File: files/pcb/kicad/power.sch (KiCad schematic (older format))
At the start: 27 parts

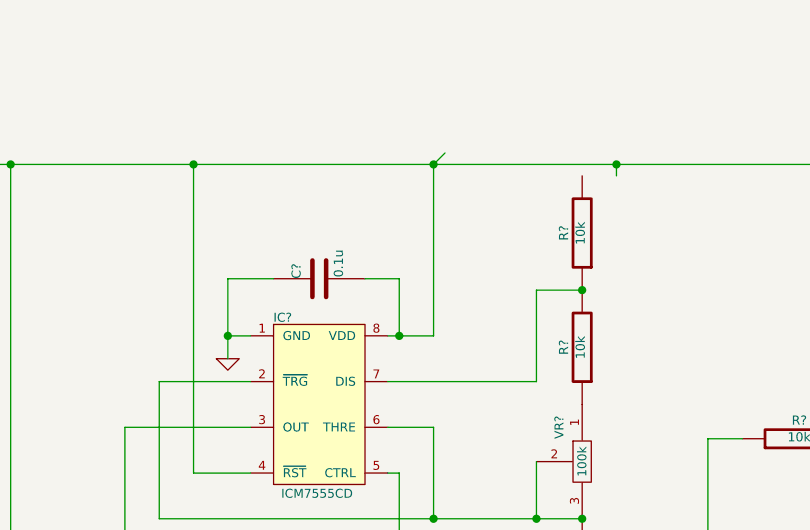
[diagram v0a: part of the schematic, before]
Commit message: 回路図更新
温度湿度センサ
大気圧センサ
輝度センサ
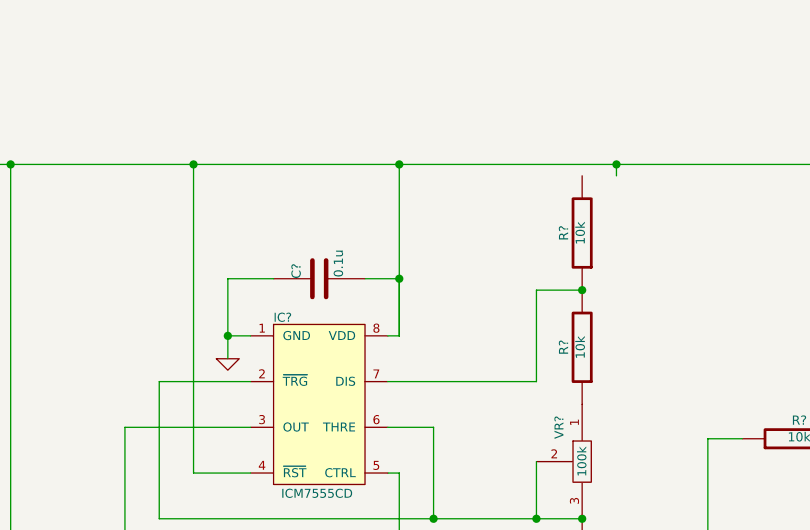
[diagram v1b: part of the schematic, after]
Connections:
- wire segments 96 -> 95
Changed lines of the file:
@@
 $EndComp
 Wire Wire Line
-	5000 3200 5000 2450
-Wire Wire Line
-	5000 2450 5050 2400
+	4850 3200 4850 2450
 Wire Wire Line
 	2650 2450 2800 2450
@@
 	3150 2450 3950 2450
 Wire Wire Line
-	3950 2450 5000 2450
-Wire Wire Line
-	5000 2450 5800 2450
+	3950 2450 4850 2450
+Wire Wire Line
+	4850 2450 5800 2450
 Wire Wire Line
 	5800 2450 7500 2450
@@
 	4800 3200 4850 3200
 Wire Wire Line
-	4850 3200 5000 3200
+	4850 3200 4850 3200
 Wire Wire Line
 	4850 3800 4800 3800
@@
 Wire Wire Line
 	5450 3400 4800 3400
-Connection ~ 4850 3200
 $Comp
 L 2SC T?
@@
 	0    -1   -1   0
 $EndComp
-Connection ~ 5000 2450
+Connection ~ 4850 2450
 Wire Wire Line
 	6350 3650 6200 3650
@@
 Connection ~ 3950 2450
 Connection ~ 5650 4400
+Connection ~ 4850 2950
 $EndSCHEMATC

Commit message: 回路図更新、DS1307対応
バスの接続が未
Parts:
- gave numbers to parts that had none: 27
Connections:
- wire segments 95 -> 97

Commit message: 回路図ERC途中
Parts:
- removed V1: 170V, symbol 170V
- added U15: DC_JACK, symbol DC_JACK
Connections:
- net labels added: 170V
- net labels removed: +9V
- wire segments 97 -> 71
- no-connect marks 0 -> 1
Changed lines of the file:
@@
 $Descr A4 11693 8268
 encoding utf-8
-Sheet 4 13
+Sheet 5 13
 Title ""
-Date "24 aug 2014"
+Date "25 aug 2014"
 Rev ""
 Comp ""
@@
 Comment4 ""
 $EndDescr
-$Comp
-L GND #PWR29
-U 1 1 53F89A11
-P 4100 3300
-F 0 "#PWR29" H 4100 3300 30  0001 C CNN
-F 1 "GND" H 4100 3230 30  0001 C CNN
-F 2 "" H 4100 3300 60  0000 C CNN
-F 3 "" H 4100 3300 60  0000 C CNN
-	1    4100 3300
-	1    0    0    -1
-$EndComp
 $Comp
 L C C8
@@
 $EndComp
 Wire Wire Line
-	4850 3200 4850 2950
-Wire Wire Line
-	4850 2950 4850 2450
-Wire Wire Line
-	2650 2450 2800 2450
-Wire Wire Line
-	2800 2450 3150 2450
-Wire Wire Line
-	3150 2450 3950 2450
-Wire Wire Line
-	3950 2450 4850 2450
-Wire Wire Line
-	4850 2450 5650 2450
-Wire Wire Line
-	5650 2450 5650 2450
-Wire Wire Line
-	5650 2450 7500 2450
-Wire Wire Line
-	7500 2450 7600 2450
+	4850 2450 4850 3200
+Wire Wire Line
+	2650 2450 7600 2450
 Wire Wire Line
 	4850 2950 4700 2950
@@
 	4300 2950 4100 2950
 Wire Wire Line
-	4100 2950 4100 3200
-Wire Wire Line
-	4100 3200 4100 3300
-Wire Wire Line
-	5650 3000 5650 3000
-Wire Wire Line
-	5650 3000 5650 3000
+	4100 2950 4100 3300
+Wire Wire Line
+	5450 3000 5650 3000
 Wire Wire Line
 	5450 4000 5450 3750
 Wire Wire Line
-	3800 4000 5000 4000
-Wire Wire Line
-	5000 4000 5450 4000
-Wire Wire Line
-	5450 4000 5650 4000
-Wire Wire Line
-	5650 4000 5650 4000
-Wire Wire Line
-	5650 4000 5650 4000
+	3800 4000 5650 4000
 Wire Wire Line
 	5650 2450 5650 2500
@@
 	5650 3500 5650 3500
 Wire Wire Line
-	4800 3200 4850 3200
-Wire Wire Line
-	4850 3200 4850 3200
+	4850 3200 4800 3200
 Wire Wire Line
 	4850 3800 4800 3800
@@
 	3650 3600 3650 4550
 Wire Wire Line
-	6900 3350 6900 3650
-Wire Wire Line
-	6900 3650 6900 3950
+	6900 3350 6900 3950
 Connection ~ 5650 4000
-Wire Wire Line
-	4850 3200 4850 2950
 Connection ~ 5650 3000
 $Comp
@@
 $EndComp
 Wire Wire Line
-	7500 3550 7500 3650
-Wire Wire Line
-	7500 3650 7500 3750
+	7500 3550 7500 3750
 Connection ~ 7500 3650
 Wire Wire Line
@@
 	7500 4200 7500 4150
 Wire Wire Line
-	7450 3650 7500 3650
-Wire Wire Line
-	7500 3650 8000 3650
+	7450 3650 8000 3650
 $Comp
 L INDUCTOR L1
@@
 Connection ~ 7500 2450
 Wire Wire Line
-	8200 2450 8300 2450
-Wire Wire Line
-	8300 2450 8400 2450
+	8200 2450 8400 2450
 Wire Wire Line
 	8300 2450 8300 3450
@@
 Connection ~ 8300 2450
 Wire Wire Line
-	8800 2450 8900 2450
-Wire Wire Line
-	8900 2450 9400 2450
-Wire Wire Line
-	9400 2450 10050 2450
+	8800 2450 10050 2450
 Wire Wire Line
 	9400 2450 9400 3450
@@
 	1    0    0    -1
 $EndComp
-Wire Wire Line
-	9400 4900 9400 3850
 $Comp
 L R R13
@@
 	8900 2450 8900 2600
 Wire Wire Line
-	8900 3650 8900 3750
-Wire Wire Line
-	8900 3750 8900 3800
+	8900 3650 8900 3800
 Wire Wire Line
 	8900 4300 8900 4350
@@
 	4850 4800 4850 3800
 Connection ~ 8900 3750
-Wire Wire Line
-	5650 3000 5450 3000
 Wire Wire Line
 	5450 3000 5450 3400
@@
 $EndComp
 $Comp
-L +9V #PWR25
-U 1 1 53F89A0B
-P 2050 2400
-F 0 "#PWR25" H 2050 2370 20  0001 C CNN
-F 1 "+9V" H 2050 2510 30  0000 C CNN
-F 2 "" H 2050 2400 60  0000 C CNN
-F 3 "" H 2050 2400 60  0000 C CNN
-	1    2050 2400
-	1    0    0    -1
-$EndComp
-$Comp
-L GND #PWR32
+L GND #PWR026
 U 1 1 53F89B53
 P 4850 5350
-F 0 "#PWR32" H 4850 5350 30  0001 C CNN
+F 0 "#PWR026" H 4850 5350 30  0001 C CNN
 F 1 "GND" H 4850 5280 30  0001 C CNN
 F 2 "" H 4850 5350 60  0000 C CNN
@@
 	4850 5200 4850 5350
 $Comp
-L GND #PWR37
+L GND #PWR027
 U 1 1 53F89C1D
 P 8900 4900
-F 0 "#PWR37" H 8900 4900 30  0001 C CNN
+F 0 "#PWR027" H 8900 4900 30  0001 C CNN
 F 1 "GND" H 8900 4830 30  0001 C CNN
 F 2 "" H 8900 4900 60  0000 C CNN
@@
 $EndComp
 $Comp
-L GND #PWR38
-U 1 1 53F89C2C
-P 9400 4900
-F 0 "#PWR38" H 9400 4900 30  0001 C CNN
-F 1 "GND" H 9400 4830 30  0001 C CNN
-F 2 "" H 9400 4900 60  0000 C CNN
-F 3 "" H 9400 4900 60  0000 C CNN
-	1    9400 4900
-	1    0    0    -1
-$EndComp
-$Comp
-L GND #PWR36
+L GND #PWR028
 U 1 1 53F89C3B
 P 8300 4200
-F 0 "#PWR36" H 8300 4200 30  0001 C CNN
+F 0 "#PWR028" H 8300 4200 30  0001 C CNN
 F 1 "GND" H 8300 4130 30  0001 C CNN
 F 2 "" H 8300 4200 60  0000 C CNN
@@
 $EndComp
 $Comp
-L GND #PWR35
+L GND #PWR029
 U 1 1 53F89C4A
 P 7500 4200
-F 0 "#PWR35" H 7500 4200 30  0001 C CNN
+F 0 "#PWR029" H 7500 4200 30  0001 C CNN
 F 1 "GND" H 7500 4130 30  0001 C CNN
 F 2 "" H 7500 4200 60  0000 C CNN
@@
 	1    0    0    -1
 $EndComp
-$Comp
-L GND #PWR34
-U 1 1 53F89C59
-P 5650 4400
-F 0 "#PWR34" H 5650 4400 30  0001 C CNN
-F 1 "GND" H 5650 4330 30  0001 C CNN
-F 2 "" H 5650 4400 60  0000 C CNN
-F 3 "" H 5650 4400 60  0000 C CNN
-	1    5650 4400
-	1    0    0    -1
-$EndComp
 Wire Wire Line
 	3950 3800 4200 3800
@@
 Connection ~ 9400 2450
 Wire Wire Line
-	6850 3650 6900 3650
-Wire Wire Line
-	6900 3650 6950 3650
+	6850 3650 6950 3650
 Connection ~ 6900 3650
 Wire Wire Line
@@
 	6200 3650 6200 4550
 $Comp
-L 170V V1
-U 1 1 53F8BBF6
-P 10050 2400
-F 0 "V1" H 10050 2400 60  0001 C CNN
-F 1 "170V" H 10060 2500 60  0000 C CNN
-F 2 "" H 10050 2400 60  0000 C CNN
-F 3 "" H 10050 2400 60  0000 C CNN
-	1    10050 2400
-	1    0    0    -1
-$EndComp
-$Comp
 L 3-TERMINAL_REGULATOR IC2
 U 1 1 53F8BD05
@@
 $EndComp
 $Comp
-L GND #PWR28
+L GND #PWR030
 U 1 1 53F8BD14
 P 3900 6450
-F 0 "#PWR28" H 3900 6450 30  0001 C CNN
+F 0 "#PWR030" H 3900 6450 30  0001 C CNN
 F 1 "GND" H 3900 6380 30  0001 C CNN
 F 2 "" H 3900 6450 60  0000 C CNN
@@
 $EndComp
 Wire Wire Line
-	4300 5950 4350 5950
-Wire Wire Line
-	4350 5950 4650 5950
-Wire Wire Line
-	4650 5950 4850 5950
+	4300 5950 4850 5950
 Wire Wire Line
 	4350 5950 4350 6000
@@
 Connection ~ 4350 5950
 Wire Wire Line
-	3150 5950 3450 5950
-Wire Wire Line
-	3450 5950 3500 5950
+	3150 5950 3500 5950
 Wire Wire Line
 	3450 5950 3450 6000
 Connection ~ 3450 5950
 $Comp
-L GND #PWR31
+L GND #PWR031
 U 1 1 53F8BED7
 P 4650 6450
-F 0 "#PWR31" H 4650 6450 30  0001 C CNN
+F 0 "#PWR031" H 4650 6450 30  0001 C CNN
 F 1 "GND" H 4650 6380 30  0001 C CNN
 F 2 "" H 4650 6450 60  0000 C CNN
@@
 $EndComp
 $Comp
-L GND #PWR30
+L GND #PWR032
 U 1 1 53F8BEE6
 P 4350 6450
-F 0 "#PWR30" H 4350 6450 30  0001 C CNN
+F 0 "#PWR032" H 4350 6450 30  0001 C CNN
 F 1 "GND" H 4350 6380 30  0001 C CNN
 F 2 "" H 4350 6450 60  0000 C CNN
@@
 $EndComp
 $Comp
-L GND #PWR27
+L GND #PWR033
 U 1 1 53F8BEF5
 P 3450 6450
-F 0 "#PWR27" H 3450 6450 30  0001 C CNN
+F 0 "#PWR033" H 3450 6450 30  0001 C CNN
 F 1 "GND" H 3450 6380 30  0001 C CNN
 F 2 "" H 3450 6450 60  0000 C CNN
@@
 $EndComp
 $Comp
-L GND #PWR26
+L GND #PWR034
 U 1 1 53F8BF04
 P 2800 3250
-F 0 "#PWR26" H 2800 3250 30  0001 C CNN
+F 0 "#PWR034" H 2800 3250 30  0001 C CNN
 F 1 "GND" H 2800 3180 30  0001 C CNN
 F 2 "" H 2800 3250 60  0000 C CNN
@@
 Connection ~ 4650 5950
 $Comp
-L +5V #PWR33
+L +5V #PWR035
 U 1 1 53F8C12B
 P 4850 5850
-F 0 "#PWR33" H 4850 5940 20  0001 C CNN
+F 0 "#PWR035" H 4850 5940 20  0001 C CNN
 F 1 "+5V" H 4850 5940 30  0000 C CNN
 F 2 "" H 4850 5850 60  0000 C CNN
@@
 $EndComp
 Wire Wire Line
-	2150 2450 2050 2450
-Wire Wire Line
-	2050 2450 2050 2400
-Wire Wire Line
 	3150 5950 3150 2450
 Connection ~ 3150 2450
@@
 	3950 3800 3950 2450
 Connection ~ 3950 2450
-Connection ~ 5650 4400
 Connection ~ 4850 2950
+$Comp
+L DC_JACK U15
+U 1 1 53FB6A7A
+P 1500 2550
+F 0 "U15" H 1350 2725 60  0000 C CNN
+F 1 "DC_JACK" H 1500 2375 60  0000 C CNN
+F 2 "" H 1350 2725 60  0000 C CNN
+F 3 "" H 1350 2725 60  0000 C CNN
+	1    1500 2550
+	1    0    0    -1
+$EndComp
+Wire Wire Line
+	1850 2650 1850 3150
+Wire Wire Line
+	1850 3150 2800 3150
+Connection ~ 2800 3150
+NoConn ~ 1850 2550
+$Comp
+L GND #PWR036
+U 1 1 53FBE781
+P 9400 4200
+F 0 "#PWR036" H 9400 4200 30  0001 C CNN
+F 1 "GND" H 9400 4130 30  0001 C CNN
+F 2 "" H 9400 4200 60  0000 C CNN
+F 3 "" H 9400 4200 60  0000 C CNN
+	1    9400 4200
+	1    0    0    -1
+$EndComp
+Wire Wire Line
+	9400 3850 9400 4200
+Text GLabel 10050 2450 2    60   Input ~ 0
+170V
+$Comp
+L GND #PWR037
+U 1 1 53FBF18E
+P 4100 3300
+F 0 "#PWR037" H 4100 3300 30  0001 C CNN
+F 1 "GND" H 4100 3230 30  0001 C CNN
+F 2 "" H 4100 3300 60  0000 C CNN
+F 3 "" H 4100 3300 60  0000 C CNN
+	1    4100 3300
+	1    0    0    -1
+$EndComp
+$Comp
+L GND #PWR038
+U 1 1 53FBF1A0
+P 5650 4450
+F 0 "#PWR038" H 5650 4450 30  0001 C CNN
+F 1 "GND" H 5650 4380 30  0001 C CNN
+F 2 "" H 5650 4450 60  0000 C CNN
+F 3 "" H 5650 4450 60  0000 C CNN
+	1    5650 4450
+	1    0    0    -1
+$EndComp
+Wire Wire Line
+	5650 4400 5650 4450
+Wire Wire Line
+	1850 2450 2150 2450
 $EndSCHEMATC

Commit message: 回路図ERC完了
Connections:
- net labels added: +9V
- wire segments 71 -> 76
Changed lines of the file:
@@
 Sheet 5 13
 Title ""
-Date "25 aug 2014"
+Date "26 aug 2014"
 Rev ""
 Comp ""
@@
 $EndComp
 $Comp
-L GND #PWR026
+L GND #PWR028
 U 1 1 53F89B53
 P 4850 5350
-F 0 "#PWR026" H 4850 5350 30  0001 C CNN
+F 0 "#PWR028" H 4850 5350 30  0001 C CNN
 F 1 "GND" H 4850 5280 30  0001 C CNN
 F 2 "" H 4850 5350 60  0000 C CNN
@@
 	4850 5200 4850 5350
 $Comp
-L GND #PWR027
+L GND #PWR029
 U 1 1 53F89C1D
 P 8900 4900
-F 0 "#PWR027" H 8900 4900 30  0001 C CNN
+F 0 "#PWR029" H 8900 4900 30  0001 C CNN
 F 1 "GND" H 8900 4830 30  0001 C CNN
 F 2 "" H 8900 4900 60  0000 C CNN
@@
 $EndComp
 $Comp
-L GND #PWR028
+L GND #PWR030
 U 1 1 53F89C3B
 P 8300 4200
-F 0 "#PWR028" H 8300 4200 30  0001 C CNN
+F 0 "#PWR030" H 8300 4200 30  0001 C CNN
 F 1 "GND" H 8300 4130 30  0001 C CNN
 F 2 "" H 8300 4200 60  0000 C CNN
@@
 $EndComp
 $Comp
-L GND #PWR029
+L GND #PWR031
 U 1 1 53F89C4A
 P 7500 4200
-F 0 "#PWR029" H 7500 4200 30  0001 C CNN
+F 0 "#PWR031" H 7500 4200 30  0001 C CNN
 F 1 "GND" H 7500 4130 30  0001 C CNN
 F 2 "" H 7500 4200 60  0000 C CNN
@@
 $EndComp
 $Comp
-L GND #PWR030
+L GND #PWR032
 U 1 1 53F8BD14
 P 3900 6450
-F 0 "#PWR030" H 3900 6450 30  0001 C CNN
+F 0 "#PWR032" H 3900 6450 30  0001 C CNN
 F 1 "GND" H 3900 6380 30  0001 C CNN
 F 2 "" H 3900 6450 60  0000 C CNN
@@
 Connection ~ 3450 5950
 $Comp
-L GND #PWR031
+L GND #PWR033
 U 1 1 53F8BED7
 P 4650 6450
-F 0 "#PWR031" H 4650 6450 30  0001 C CNN
+F 0 "#PWR033" H 4650 6450 30  0001 C CNN
 F 1 "GND" H 4650 6380 30  0001 C CNN
 F 2 "" H 4650 6450 60  0000 C CNN
@@
 $EndComp
 $Comp
-L GND #PWR032
+L GND #PWR034
 U 1 1 53F8BEE6
 P 4350 6450
-F 0 "#PWR032" H 4350 6450 30  0001 C CNN
+F 0 "#PWR034" H 4350 6450 30  0001 C CNN
 F 1 "GND" H 4350 6380 30  0001 C CNN
 F 2 "" H 4350 6450 60  0000 C CNN
@@
 $EndComp
 $Comp
-L GND #PWR033
+L GND #PWR035
 U 1 1 53F8BEF5
 P 3450 6450
-F 0 "#PWR033" H 3450 6450 30  0001 C CNN
+F 0 "#PWR035" H 3450 6450 30  0001 C CNN
 F 1 "GND" H 3450 6380 30  0001 C CNN
 F 2 "" H 3450 6450 60  0000 C CNN
@@
 $EndComp
 $Comp
-L GND #PWR034
+L GND #PWR036
 U 1 1 53F8BF04
 P 2800 3250
-F 0 "#PWR034" H 2800 3250 30  0001 C CNN
+F 0 "#PWR036" H 2800 3250 30  0001 C CNN
 F 1 "GND" H 2800 3180 30  0001 C CNN
 F 2 "" H 2800 3250 60  0000 C CNN
@@
 Connection ~ 4650 5950
 $Comp
-L +5V #PWR035
+L +5V #PWR037
 U 1 1 53F8C12B
 P 4850 5850
-F 0 "#PWR035" H 4850 5940 20  0001 C CNN
+F 0 "#PWR037" H 4850 5940 20  0001 C CNN
 F 1 "+5V" H 4850 5940 30  0000 C CNN
 F 2 "" H 4850 5850 60  0000 C CNN
@@
 NoConn ~ 1850 2550
 $Comp
-L GND #PWR036
+L GND #PWR038
 U 1 1 53FBE781
 P 9400 4200
-F 0 "#PWR036" H 9400 4200 30  0001 C CNN
+F 0 "#PWR038" H 9400 4200 30  0001 C CNN
 F 1 "GND" H 9400 4130 30  0001 C CNN
 F 2 "" H 9400 4200 60  0000 C CNN
@@
 170V
 $Comp
-L GND #PWR037
+L GND #PWR039
 U 1 1 53FBF18E
 P 4100 3300
-F 0 "#PWR037" H 4100 3300 30  0001 C CNN
+F 0 "#PWR039" H 4100 3300 30  0001 C CNN
 F 1 "GND" H 4100 3230 30  0001 C CNN
 F 2 "" H 4100 3300 60  0000 C CNN
@@
 $EndComp
 $Comp
-L GND #PWR038
+L GND #PWR040
 U 1 1 53FBF1A0
 P 5650 4450
-F 0 "#PWR038" H 5650 4450 30  0001 C CNN
+F 0 "#PWR040" H 5650 4450 30  0001 C CNN
 F 1 "GND" H 5650 4380 30  0001 C CNN
 F 2 "" H 5650 4450 60  0000 C CNN
@@
 Wire Wire Line
 	1850 2450 2150 2450
+$Comp
+L +9V #PWR041
+U 1 1 53FCA114
+P 2000 2350
+F 0 "#PWR041" H 2000 2320 20  0001 C CNN
+F 1 "+9V" H 2000 2460 30  0000 C CNN
+F 2 "" H 2000 2350 60  0000 C CNN
+F 3 "" H 2000 2350 60  0000 C CNN
+	1    2000 2350
+	1    0    0    -1
+$EndComp
+Wire Wire Line
+	2000 2350 2000 2450
+Connection ~ 2000 2450
+$Comp
+L +9V #PWR042
+U 1 1 53FC9A5B
+P 1550 3500
+F 0 "#PWR042" H 1550 3470 20  0001 C CNN
+F 1 "+9V" H 1550 3610 30  0000 C CNN
+F 2 "" H 1550 3500 60  0000 C CNN
+F 3 "" H 1550 3500 60  0000 C CNN
+	1    1550 3500
+	1    0    0    -1
+$EndComp
+$Comp
+L PWR_FLAG #FLG043
+U 1 1 53FC9A79
+P 1950 3500
+F 0 "#FLG043" H 1950 3595 30  0001 C CNN
+F 1 "PWR_FLAG" H 1950 3680 30  0000 C CNN
+F 2 "" H 1950 3500 60  0000 C CNN
+F 3 "" H 1950 3500 60  0000 C CNN
+	1    1950 3500
+	1    0    0    -1
+$EndComp
+$Comp
+L GND #PWR044
+U 1 1 53FC9AEE
+P 1950 3550
+F 0 "#PWR044" H 1950 3550 30  0001 C CNN
+F 1 "GND" H 1950 3480 30  0001 C CNN
+F 2 "" H 1950 3550 60  0000 C CNN
+F 3 "" H 1950 3550 60  0000 C CNN
+	1    1950 3550
+	1    0    0    -1
+$EndComp
+$Comp
+L PWR_FLAG #FLG045
+U 1 1 53FC9AFB
+P 1700 3500
+F 0 "#FLG045" H 1700 3595 30  0001 C CNN
+F 1 "PWR_FLAG" H 1700 3680 30  0000 C CNN
+F 2 "" H 1700 3500 60  0000 C CNN
+F 3 "" H 1700 3500 60  0000 C CNN
+	1    1700 3500
+	1    0    0    -1
+$EndComp
+Wire Wire Line
+	1950 3500 1950 3550
+Wire Wire Line
+	1550 3500 1550 3550
+Wire Wire Line
+	1550 3550 1700 3550
+Wire Wire Line
+	1700 3550 1700 3500
 $EndSCHEMATC

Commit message: 部品リスト・パッケージライブラリを更新
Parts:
- renumbered C8 to C10, C9 to C11, C10 to C12, C11 to C13, C5 to C7, C6 to C8, C7 to C9, D3 to D2, IC4 to IC10, IC2 to IC8, IC3 to IC9, R8 to R12, R9 to R13, R10 to R14, R11 to R15, R12 to R16, R13 to R17, R14 to R18, R15 to R19, U15 to U11
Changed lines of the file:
@@
 $EndDescr
 $Comp
-L C C8
+L C C10
 U 1 1 53F89A17
 P 4500 2950
-F 0 "C8" H 4500 3050 40  0000 L CNN
+F 0 "C10" H 4500 3050 40  0000 L CNN
 F 1 "0.1u" H 4506 2865 40  0000 L CNN
 F 2 "~" H 4538 2800 30  0000 C CNN
@@
 $EndComp
 $Comp
-L R R8
+L R R12
 U 1 1 53F89A1D
 P 5650 2750
-F 0 "R8" V 5730 2750 40  0000 C CNN
+F 0 "R12" V 5730 2750 40  0000 C CNN
 F 1 "10k" V 5657 2751 40  0000 C CNN
 F 2 "~" V 5580 2750 30  0000 C CNN
@@
 $EndComp
 $Comp
-L R R9
+L R R13
 U 1 1 53F89A23
 P 5650 3250
-F 0 "R9" V 5730 3250 40  0000 C CNN
+F 0 "R13" V 5730 3250 40  0000 C CNN
 F 1 "10k" V 5657 3251 40  0000 C CNN
 F 2 "~" V 5580 3250 30  0000 C CNN
@@
 $EndComp
 $Comp
-L ICM7555CD IC3
+L ICM7555CD IC9
 U 1 1 53F89A2F
 P 4500 3500
-F 0 "IC3" H 4340 3880 39  0000 C CNN
+F 0 "IC9" H 4340 3880 39  0000 C CNN
 F 1 "ICM7555CD" H 4490 3110 39  0000 C CNN
 F 2 "~" H 4400 3500 60  0000 C CNN
@@
 $EndComp
 $Comp
-L C C10
+L C C12
 U 1 1 53F89A35
 P 5650 4200
-F 0 "C10" H 5650 4300 40  0000 L CNN
+F 0 "C12" H 5650 4300 40  0000 L CNN
 F 1 "1000p" H 5656 4115 40  0000 L CNN
 F 2 "~" H 5688 4050 30  0000 C CNN
@@
 Connection ~ 5650 3000
 $Comp
-L R R12
+L R R16
 U 1 1 53F89A5A
 P 7500 2800
-F 0 "R12" V 7580 2800 40  0000 C CNN
+F 0 "R16" V 7580 2800 40  0000 C CNN
 F 1 "4.7k" V 7507 2801 40  0000 C CNN
 F 2 "~" V 7430 2800 30  0000 C CNN
@@
 $EndComp
 $Comp
-L R R11
+L R R15
 U 1 1 53F89A60
 P 7200 3650
-F 0 "R11" V 7300 3650 40  0000 C CNN
+F 0 "R15" V 7300 3650 40  0000 C CNN
 F 1 "10K" V 7207 3651 40  0000 C CNN
 F 2 "~" V 7130 3650 30  0000 C CNN
@@
 	8300 4200 8300 3850
 $Comp
-L DIODE D3
+L DIODE D2
 U 1 1 53F89A7D
 P 8600 2450
-F 0 "D3" H 8600 2550 40  0000 C CNN
+F 0 "D2" H 8600 2550 40  0000 C CNN
 F 1 "DIODE" H 8600 2350 40  0000 C CNN
 F 2 "~" H 8600 2450 60  0000 C CNN
@@
 	9400 2450 9400 3450
 $Comp
-L C C11
+L C C13
 U 1 1 53F89A86
 P 9400 3650
-F 0 "C11" H 9400 3750 40  0000 L CNN
+F 0 "C13" H 9400 3750 40  0000 L CNN
 F 1 "350V 1u" H 9406 3565 40  0000 L CNN
 F 2 "~" H 9438 3500 30  0000 C CNN
@@
 $EndComp
 $Comp
-L R R13
+L R R17
 U 1 1 53F89A8E
 P 8900 2850
-F 0 "R13" V 8980 2850 40  0000 C CNN
+F 0 "R17" V 8980 2850 40  0000 C CNN
 F 1 "500k" V 8907 2851 40  0000 C CNN
 F 2 "~" V 8830 2850 30  0000 C CNN
@@
 $EndComp
 $Comp
-L R R14
+L R R18
 U 1 1 53F89A94
 P 8900 3400
-F 0 "R14" V 8980 3400 40  0000 C CNN
+F 0 "R18" V 8980 3400 40  0000 C CNN
 F 1 "500k" V 8907 3401 40  0000 C CNN
 F 2 "~" V 8830 3400 30  0000 C CNN
@@
 $EndComp
 $Comp
-L R R15
+L R R19
 U 1 1 53F89A9A
 P 8900 4050
-F 0 "R15" V 8980 4050 40  0000 C CNN
+F 0 "R19" V 8980 4050 40  0000 C CNN
 F 1 "10k" V 8907 4051 40  0000 C CNN
 F 2 "~" V 8830 4050 30  0000 C CNN
@@
 Connection ~ 8900 2450
 $Comp
-L FET IC4
+L FET IC10
 U 1 1 53F89AC9
 P 8200 3650
-F 0 "IC4" H 8210 3820 39  0000 R CNN
+F 0 "IC10" H 8210 3820 39  0000 R CNN
 F 1 "FET" H 8150 3500 39  0000 R CNN
 F 2 "" H 8200 3650 60  0000 C CNN
@@
 	4100 3200 4200 3200
 $Comp
-L R R10
+L R R14
 U 1 1 53F8A0A8
 P 6600 3650
-F 0 "R10" V 6500 3650 40  0000 C CNN
+F 0 "R14" V 6500 3650 40  0000 C CNN
 F 1 "10k" V 6607 3651 40  0000 C CNN
 F 2 "~" V 6530 3650 30  0000 C CNN
@@
 	6200 3650 6200 4550
 $Comp
-L 3-TERMINAL_REGULATOR IC2
+L 3-TERMINAL_REGULATOR IC8
 U 1 1 53F8BD05
 P 3900 6000
-F 0 "IC2" H 4050 5804 60  0000 C CNN
+F 0 "IC8" H 4050 5804 60  0000 C CNN
 F 1 "3-TERMINAL_REGULATOR" H 3900 6200 60  0000 C CNN
 F 2 "~" H 3900 6000 60  0000 C CNN
@@
 	3900 6250 3900 6450
 $Comp
-L C C6
+L C C8
 U 1 1 53F8BD8A
 P 3450 6200
-F 0 "C6" H 3450 6300 40  0000 L CNN
+F 0 "C8" H 3450 6300 40  0000 L CNN
 F 1 "0.1u" H 3450 6100 40  0000 L CNN
 F 2 "~" H 3488 6050 30  0000 C CNN
@@
 $EndComp
 $Comp
-L C C5
+L C C7
 U 1 1 53F8BD97
 P 2800 2900
-F 0 "C5" H 2800 3000 40  0000 L CNN
+F 0 "C7" H 2800 3000 40  0000 L CNN
 F 1 "25V 10u" H 2800 2800 40  0000 L CNN
 F 2 "~" H 2838 2750 30  0000 C CNN
@@
 $EndComp
 $Comp
-L C C9
+L C C11
 U 1 1 53F8BD9D
 P 4650 6200
-F 0 "C9" H 4650 6300 40  0000 L CNN
+F 0 "C11" H 4650 6300 40  0000 L CNN
 F 1 "25V 10u" H 4650 6100 40  0000 L CNN
 F 2 "~" H 4688 6050 30  0000 C CNN
@@
 $EndComp
 $Comp
-L C C7
+L C C9
 U 1 1 53F8BDA3
 P 4350 6200
-F 0 "C7" H 4350 6300 40  0000 L CNN
+F 0 "C9" H 4350 6300 40  0000 L CNN
 F 1 "0.1u" H 4350 6100 40  0000 L CNN
 F 2 "~" H 4388 6050 30  0000 C CNN
@@
 Connection ~ 4850 2950
 $Comp
-L DC_JACK U15
+L DC_JACK U11
 U 1 1 53FB6A7A
 P 1500 2550
-F 0 "U15" H 1350 2725 60  0000 C CNN
+F 0 "U11" H 1350 2725 60  0000 C CNN
 F 1 "DC_JACK" H 1500 2375 60  0000 C CNN
 F 2 "" H 1350 2725 60  0000 C CNN

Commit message: 部品リスト完了、PCBに部品を配置
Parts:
- removed IC8: 3-TERMINAL_REGULATOR, ~, symbol 3-TERMINAL_REGULATOR
- added IC8: MY_3_TERMINAL_REGULATOR, ~, symbol MY_3_TERMINAL_REGULATOR
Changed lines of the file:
@@
 Sheet 5 13
 Title ""
-Date "26 aug 2014"
+Date "28 aug 2014"
 Rev ""
 Comp ""
@@
 	6200 3650 6200 4550
 $Comp
-L 3-TERMINAL_REGULATOR IC8
-U 1 1 53F8BD05
-P 3900 6000
-F 0 "IC8" H 4050 5804 60  0000 C CNN
-F 1 "3-TERMINAL_REGULATOR" H 3900 6200 60  0000 C CNN
-F 2 "~" H 3900 6000 60  0000 C CNN
-F 3 "~" H 3900 6000 60  0000 C CNN
-	1    3900 6000
-	1    0    0    -1
-$EndComp
-$Comp
 L GND #PWR032
 U 1 1 53F8BD14
@@
 Wire Wire Line
 	1700 3550 1700 3500
+$Comp
+L MY_3_TERMINAL_REGULATOR IC8
+U 1 1 53FF5CD5
+P 3900 6000
+F 0 "IC8" H 4050 5804 60  0000 C CNN
+F 1 "MY_3_TERMINAL_REGULATOR" H 3900 6200 60  0000 C CNN
+F 2 "~" H 3900 6000 60  0000 C CNN
+F 3 "~" H 3900 6000 60  0000 C CNN
+	1    3900 6000
+	1    0    0    -1
+$EndComp
 $EndSCHEMATC

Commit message: PCB
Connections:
- net labels added: 5V_L, GND_L
- wire segments 76 -> 82
